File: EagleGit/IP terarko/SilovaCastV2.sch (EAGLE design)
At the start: 53 parts, among them Q1 BC557C, T1 BT138-V, T2 BT138-V, T3 BT138-V, T4 BT138-V

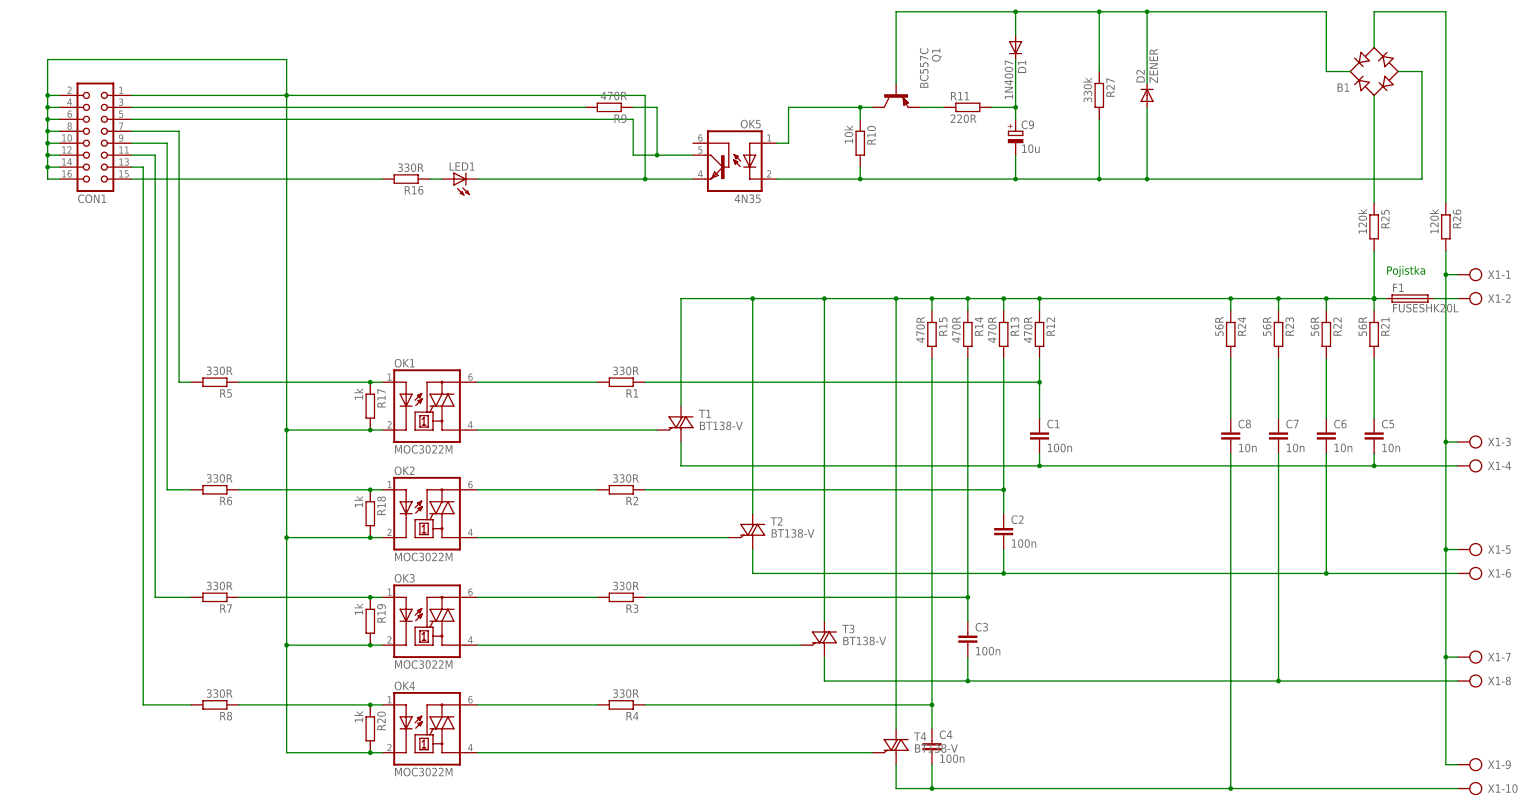
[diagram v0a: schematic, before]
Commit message: Uprava konektoru u DPS "silova cast"
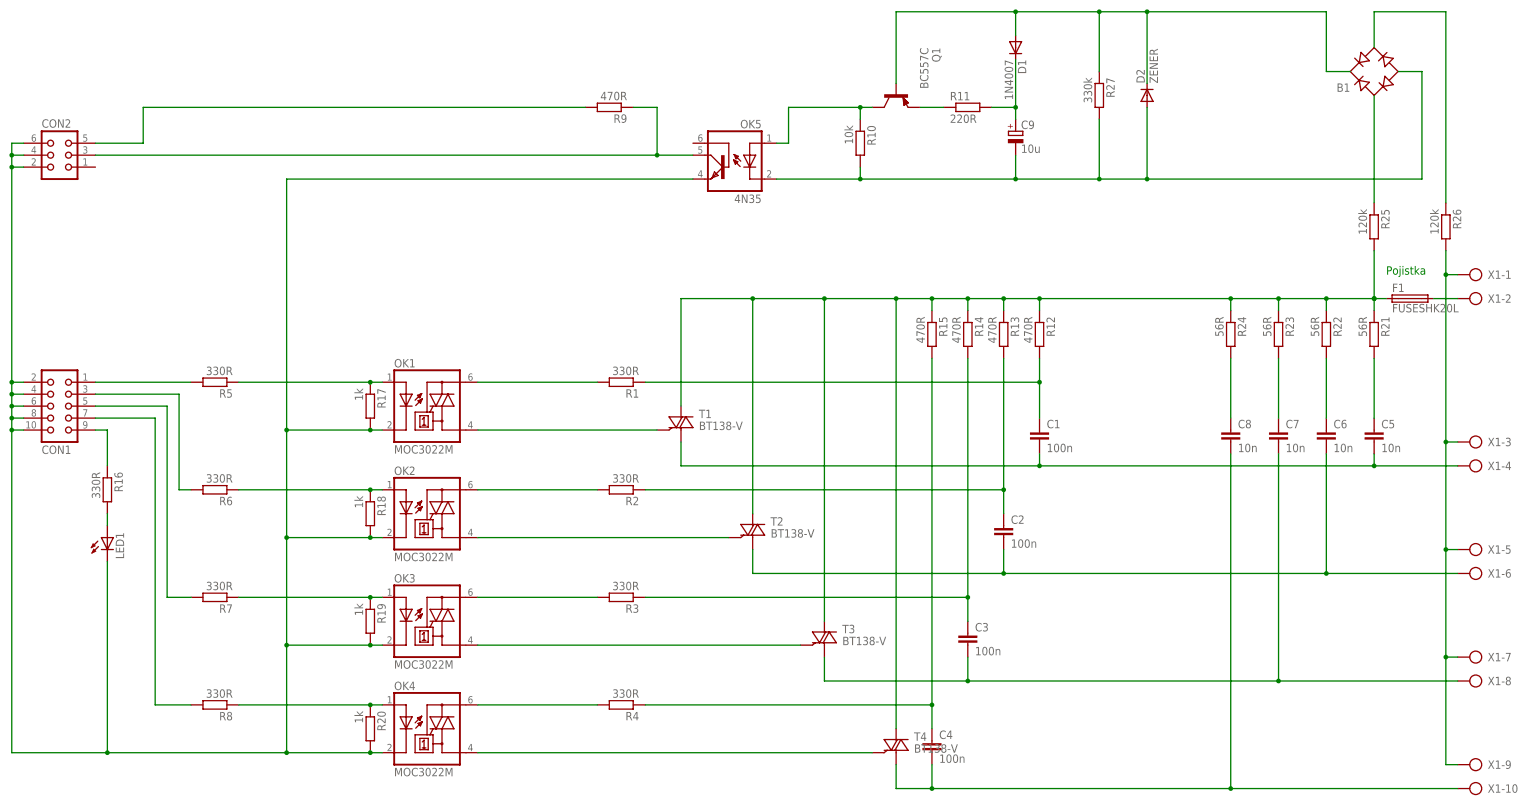
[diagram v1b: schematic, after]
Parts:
- added CON2: (no value), con-harting:CON06
- CON1: device con-harting:CON16 -> con-harting:CON10
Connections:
- removed net N$35: LED1.A, R16.1
- new net N$23: CON1.1, R5.2
- net GND: now also CON2.2, CON2.4, CON2.6; no longer CON1.1, CON1.12, CON1.14, CON1.16
- net N$17: now also CON2.5; no longer CON1.3
- net N$22: now also CON2.3; no longer CON1.5
- net N$28: now also CON1.3, R6.2; no longer CON1.7, R5.2
- net N$29: now also CON1.5, R7.2; no longer CON1.9, R6.2
- net N$30: now also CON1.7, R8.2; no longer CON1.11, R7.2
- net N$31: now also CON1.9, R16.1; no longer CON1.13, R8.2
- net N$34: now also LED1.A; no longer CON1.15
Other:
- moved on the sheet: LED1, R16
